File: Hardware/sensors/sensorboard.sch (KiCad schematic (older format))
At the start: 0 parts

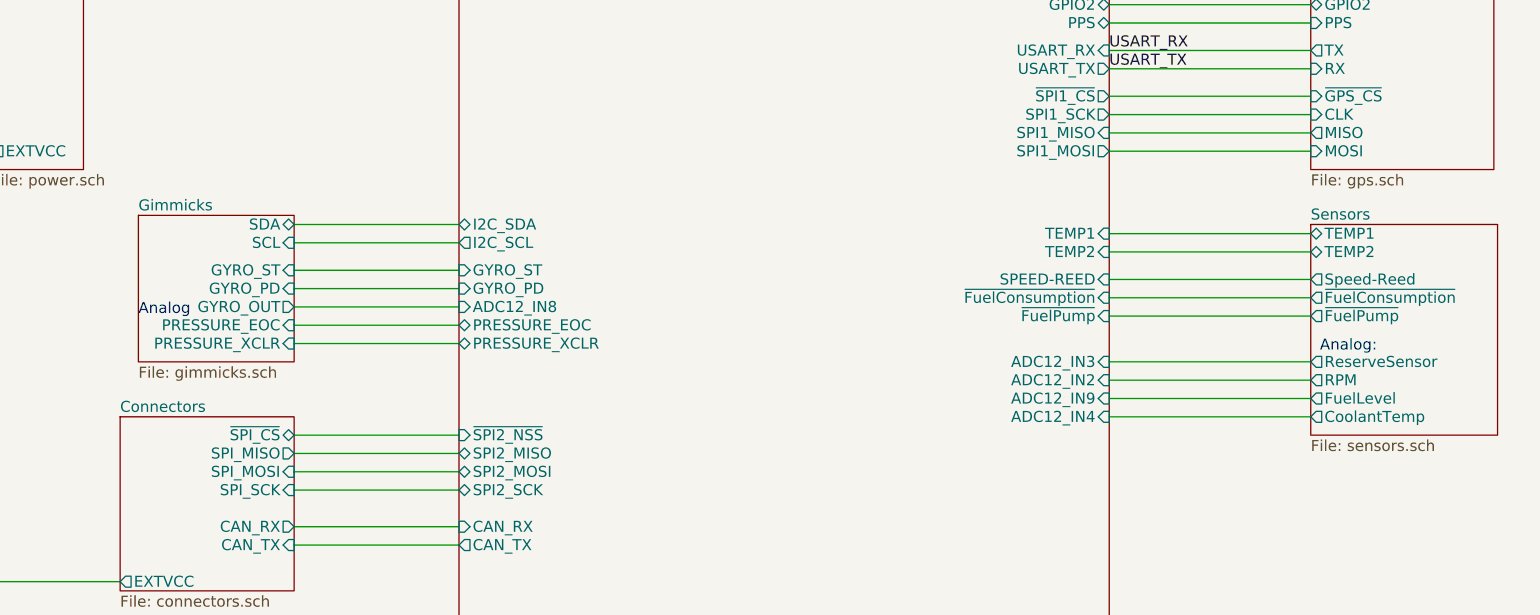
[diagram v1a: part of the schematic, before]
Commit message: sensor board first version
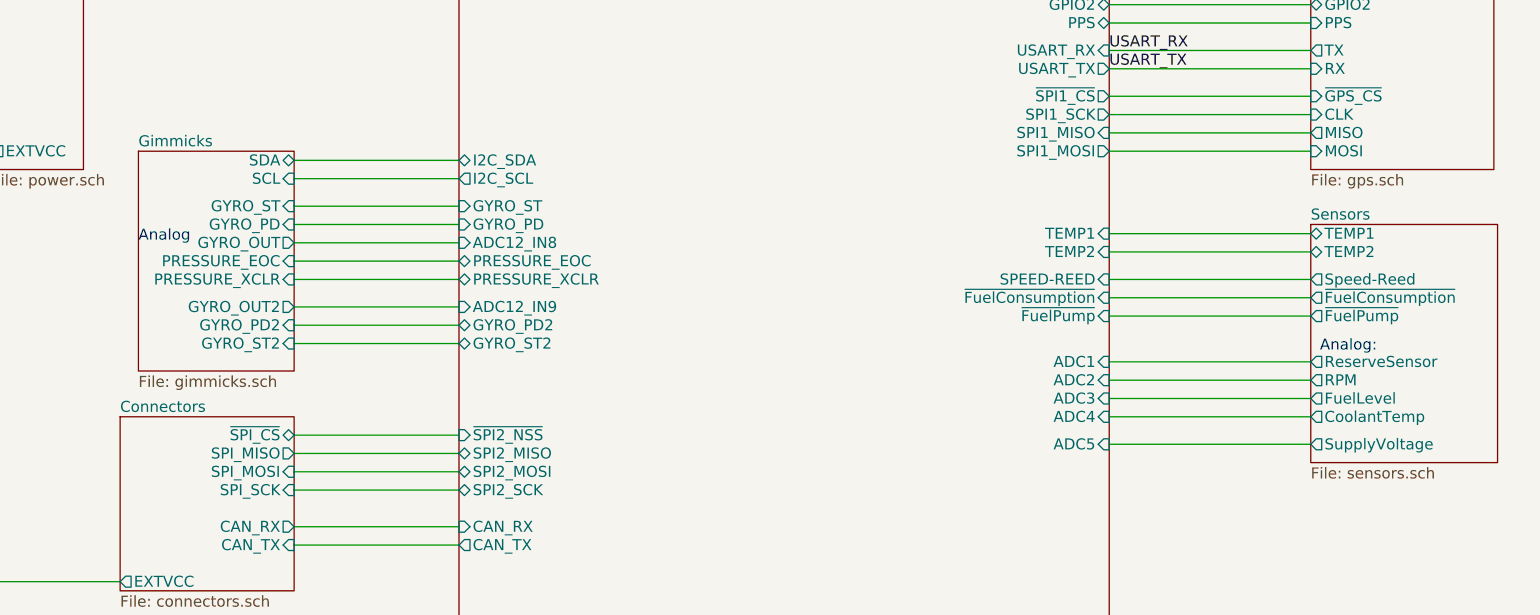
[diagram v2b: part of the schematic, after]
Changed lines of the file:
@@
-EESchema Schematic File Version 2  date Do 10 Mär 2011 16:21:43 CET
+EESchema Schematic File Version 2  date Do 17 Mär 2011 20:34:15 CET
 LIBS:power
 LIBS:device
@@
 Sheet 1 8
 Title ""
-Date "10 mar 2011"
+Date "17 mar 2011"
 Rev ""
 Comp ""
@@
 $EndDescr
 Wire Wire Line
+	7800 3400 6700 3400
+Wire Wire Line
+	2250 2500 3150 2500
+Wire Wire Line
+	2250 2400 3150 2400
+Wire Wire Line
+	2250 2300 3150 2300
+Wire Wire Line
+	2250 2200 3150 2200
+Wire Wire Line
+	2250 2100 3150 2100
+Wire Wire Line
+	6700 2700 7800 2700
+Wire Wire Line
+	6700 2600 7800 2600
+Wire Wire Line
+	6700 2500 7800 2500
+Wire Wire Line
+	6700 2350 7800 2350
+Wire Wire Line
+	6700 2250 7800 2250
+Wire Wire Line
+	6700 1800 7800 1800
+Wire Wire Line
+	6700 1700 7800 1700
+Wire Wire Line
+	6700 1600 7800 1600
+Wire Wire Line
+	6700 1500 7800 1500
+Wire Wire Line
+	2250 5550 3150 5550
+Wire Wire Line
+	2250 5450 3150 5450
+Wire Wire Line
+	2250 5350 3150 5350
+Wire Wire Line
+	2250 5250 3150 5250
+Wire Wire Line
+	2250 5150 3150 5150
+Wire Wire Line
+	2250 5050 3150 5050
+Wire Wire Line
+	2250 3650 3150 3650
+Wire Wire Line
+	2250 3550 3150 3550
+Wire Wire Line
+	2250 3450 3150 3450
+Wire Wire Line
+	2250 3350 3150 3350
+Wire Wire Line
+	6700 3250 7800 3250
+Wire Wire Line
+	6700 3150 7800 3150
+Wire Wire Line
+	6700 3050 7800 3050
+Wire Wire Line
+	6700 2950 7800 2950
+Wire Wire Line
+	2250 3850 3150 3850
+Wire Wire Line
+	2250 3950 3150 3950
+Wire Wire Line
+	600  1800 550  1800
+Wire Wire Line
+	550  1800 550  4150
+Wire Wire Line
+	550  4150 1300 4150
+Wire Wire Line
+	6700 1250 7800 1250
+Wire Wire Line
+	6700 1350 7800 1350
+Wire Wire Line
+	6700 800  7800 800
+Wire Wire Line
+	6700 900  7800 900
+Wire Wire Line
+	6700 1000 7800 1000
+Wire Wire Line
+	6700 1100 7800 1100
+Wire Wire Line
+	2250 1850 3150 1850
+Wire Wire Line
+	2250 1950 3150 1950
+Wire Wire Line
+	2250 2650 3150 2650
+Wire Wire Line
+	2250 2750 3150 2750
+Wire Wire Line
 	2250 2850 3150 2850
-Wire Wire Line
-	2250 2750 3150 2750
-Wire Wire Line
-	6700 2700 7800 2700
-Wire Wire Line
-	6700 2600 7800 2600
-Wire Wire Line
-	6700 2500 7800 2500
-Wire Wire Line
-	6700 2350 7800 2350
-Wire Wire Line
-	6700 2250 7800 2250
-Wire Wire Line
-	6700 1800 7800 1800
-Wire Wire Line
-	6700 1700 7800 1700
-Wire Wire Line
-	6700 1600 7800 1600
-Wire Wire Line
-	6700 1500 7800 1500
-Wire Wire Line
-	2250 5550 3150 5550
-Wire Wire Line
-	2250 5450 3150 5450
-Wire Wire Line
-	2250 5350 3150 5350
-Wire Wire Line
-	2250 5250 3150 5250
-Wire Wire Line
-	2250 5150 3150 5150
-Wire Wire Line
-	2250 5050 3150 5050
-Wire Wire Line
-	2250 3650 3150 3650
-Wire Wire Line
-	2250 3550 3150 3550
-Wire Wire Line
-	2250 3450 3150 3450
-Wire Wire Line
-	2250 3350 3150 3350
-Wire Wire Line
-	6700 3250 7800 3250
-Wire Wire Line
-	6700 3150 7800 3150
-Wire Wire Line
-	6700 3050 7800 3050
-Wire Wire Line
-	6700 2950 7800 2950
-Wire Wire Line
-	2250 3850 3150 3850
-Wire Wire Line
-	2250 3950 3150 3950
-Wire Wire Line
-	3150 2650 2250 2650
-Wire Wire Line
-	600  1800 550  1800
-Wire Wire Line
-	550  1800 550  4150
-Wire Wire Line
-	550  4150 1300 4150
-Wire Wire Line
-	3150 2200 2250 2200
-Wire Wire Line
-	3150 2300 2250 2300
-Wire Wire Line
-	6700 1250 7800 1250
-Wire Wire Line
-	6700 1350 7800 1350
-Wire Wire Line
-	6700 800  7800 800
-Wire Wire Line
-	6700 900  7800 900
-Wire Wire Line
-	6700 1000 7800 1000
-Wire Wire Line
-	6700 1100 7800 1100
-Wire Wire Line
-	2250 2450 3150 2450
-Wire Wire Line
-	2250 2550 3150 2550
 Text Label 2250 5750 0    60   ~ 0
 USART_TX
@@
 F9 "JTMS" O R 2250 5550 60
 $EndSheet
-Text Notes 1400 2700 0    60   ~ 0
+Text Notes 1400 2300 0    60   ~ 0
 Analog
 Text Notes 7850 2900 0    60   ~ 0
@@
 F0 "MCU" 60
 F1 "mcu.sch" 60
-F2 "ADC12_IN8" I L 3150 2650 60
-F3 "ADC12_IN4" I R 6700 3250 60
-F4 "NRST" I L 3150 5050 60
-F5 "JTDI" I L 3150 5350 60
-F6 "JTCK" I L 3150 5450 60
-F7 "JTMS" I L 3150 5550 60
-F8 "CAN_TX" O L 3150 3950 60
-F9 "CAN_RX" I L 3150 3850 60
-F10 "~SPI1_CS" O R 6700 1500 60
-F11 "SPI1_MOSI" O R 6700 1800 60
-F12 "SPI1_MISO" I R 6700 1700 60
-F13 "SPI1_SCK" O R 6700 1600 60
-F14 "ADC12_IN3" I R 6700 2950 60
-F15 "ADC12_IN2" I R 6700 3050 60
-F16 "ADC12_IN9" I R 6700 3150 60
-F17 "SPI2_MOSI" B L 3150 3550 60
-F18 "SPI2_MISO" B L 3150 3450 60
-F19 "SPI2_SCK" B L 3150 3650 60
-F20 "~SPI2_NSS" I L 3150 3350 60
-F21 "I2C_SDA" B L 3150 2200 60
-F22 "I2C_SCL" O L 3150 2300 60
-F23 "USART_RX" I R 6700 1250 60
-F24 "USART_TX" O R 6700 1350 60
-F25 "TEMP1" I R 6700 2250 60
-F26 "TEMP2" I R 6700 2350 60
-F27 "GPIO2" B R 6700 1000 60
-F28 "GPIO1" B R 6700 900 60
-F29 "GPIO20" B R 6700 800 60
-F30 "PPS" B R 6700 1100 60
-F31 "~FuelPump" I R 6700 2700 60
-F32 "~FuelConsumption" I R 6700 2600 60
-F33 "SPEED-REED" I R 6700 2500 60
-F34 "GYRO_PD" I L 3150 2550 60
-F35 "GYRO_ST" I L 3150 2450 60
-F36 "PRESSURE_XCLR" B L 3150 2850 60
-F37 "PRESSURE_EOC" B L 3150 2750 60
-F38 "JTDO" O L 3150 5250 60
-F39 "TRST" I L 3150 5150 60
+F2 "ADC12_IN8" I L 3150 2300 60
+F3 "NRST" I L 3150 5050 60
+F4 "JTDI" I L 3150 5350 60
+F5 "JTCK" I L 3150 5450 60
+F6 "JTMS" I L 3150 5550 60
+F7 "CAN_TX" O L 3150 3950 60
+F8 "CAN_RX" I L 3150 3850 60
+F9 "~SPI1_CS" O R 6700 1500 60
+F10 "SPI1_MOSI" O R 6700 1800 60
+F11 "SPI1_MISO" I R 6700 1700 60
+F12 "SPI1_SCK" O R 6700 1600 60
+F13 "ADC12_IN9" I L 3150 2650 60
+F14 "SPI2_MOSI" B L 3150 3550 60
+F15 "SPI2_MISO" B L 3150 3450 60
+F16 "SPI2_SCK" B L 3150 3650 60
+F17 "~SPI2_NSS" I L 3150 3350 60
+F18 "I2C_SDA" B L 3150 1850 60
+F19 "I2C_SCL" O L 3150 1950 60
+F20 "USART_RX" I R 6700 1250 60
+F21 "USART_TX" O R 6700 1350 60
+F22 "TEMP1" I R 6700 2250 60
+F23 "TEMP2" I R 6700 2350 60
+F24 "GPIO2" B R 6700 1000 60
+F25 "GPIO1" B R 6700 900 60
+F26 "GPIO20" B R 6700 800 60
+F27 "PPS" B R 6700 1100 60
+F28 "~FuelPump" I R 6700 2700 60
+F29 "~FuelConsumption" I R 6700 2600 60
+F30 "SPEED-REED" I R 6700 2500 60
+F31 "GYRO_PD" I L 3150 2200 60
+F32 "GYRO_ST" I L 3150 2100 60
+F33 "PRESSURE_XCLR" B L 3150 2500 60
+F34 "PRESSURE_EOC" B L 3150 2400 60
+F35 "JTDO" O L 3150 5250 60
+F36 "TRST" I L 3150 5150 60
+F37 "GYRO_ST2" B L 3150 2850 60
+F38 "GYRO_PD2" B L 3150 2750 60
+F39 "ADC5" I R 6700 3400 60
+F40 "ADC4" I R 6700 3250 60
+F41 "ADC3" I R 6700 3150 60
+F42 "ADC2" I R 6700 3050 60
+F43 "ADC1" I R 6700 2950 60
 $EndSheet
 $Sheet
@@
 $EndSheet
 $Sheet
-S 1400 2150 850  800
+S 1400 1800 850  1200
 U 4D781E1F
 F0 "Gimmicks" 60
 F1 "gimmicks.sch" 60
-F2 "SDA" B R 2250 2200 60
-F3 "SCL" I R 2250 2300 60
-F4 "GYRO_ST" I R 2250 2450 60
-F5 "GYRO_PD" I R 2250 2550 60
-F6 "GYRO_OUT" O R 2250 2650 60
-F7 "PRESSURE_EOC" I R 2250 2750 60
-F8 "PRESSURE_XCLR" I R 2250 2850 60
-$EndSheet
-$Sheet
-S 7800 2200 1020 1150
+F2 "SDA" B R 2250 1850 60
+F3 "SCL" I R 2250 1950 60
+F4 "GYRO_ST" I R 2250 2100 60
+F5 "GYRO_PD" I R 2250 2200 60
+F6 "GYRO_OUT" O R 2250 2300 60
+F7 "PRESSURE_EOC" I R 2250 2400 60
+F8 "PRESSURE_XCLR" I R 2250 2500 60
+F9 "GYRO_OUT2" O R 2250 2650 60
+F10 "GYRO_PD2" I R 2250 2750 60
+F11 "GYRO_ST2" I R 2250 2850 60
+$EndSheet
+$Sheet
+S 7800 2200 1020 1300
 U 4D781E19
 F0 "Sensors" 60
@@
 F9 "~FuelConsumption" O L 7800 2600 60
 F10 "~FuelPump" O L 7800 2700 60
-$EndSheet
-$Sheet
+F11 "SupplyVoltage" O L 7800 3400 60
+$EndSheet
+$Sheet
